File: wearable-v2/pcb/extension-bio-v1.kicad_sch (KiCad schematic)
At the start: 12 parts, among them J5 EXT_2_SOCKET, U11 TMP1075, U12 MAX30102

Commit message: Further V2 routing
Signed-off-by: Adam Fowler <adam@adamfowler.org>
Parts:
- H1: footprint Herald_Extras:MillSlot_8.0x1.0mm -> Herald:MillSlot_8.0x1.0mm
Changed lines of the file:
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@@
       (effects (font (size 1.27 1.27)) (justify left))
     )
-    (property "Footprint" "Herald_Extras:MillSlot_8.0x1.0mm" (at 78.74 171.45 0)
+    (property "Footprint" "Herald:MillSlot_8.0x1.0mm" (at 78.74 171.45 0)
       (effects (font (size 1.27 1.27)) hide)
     )

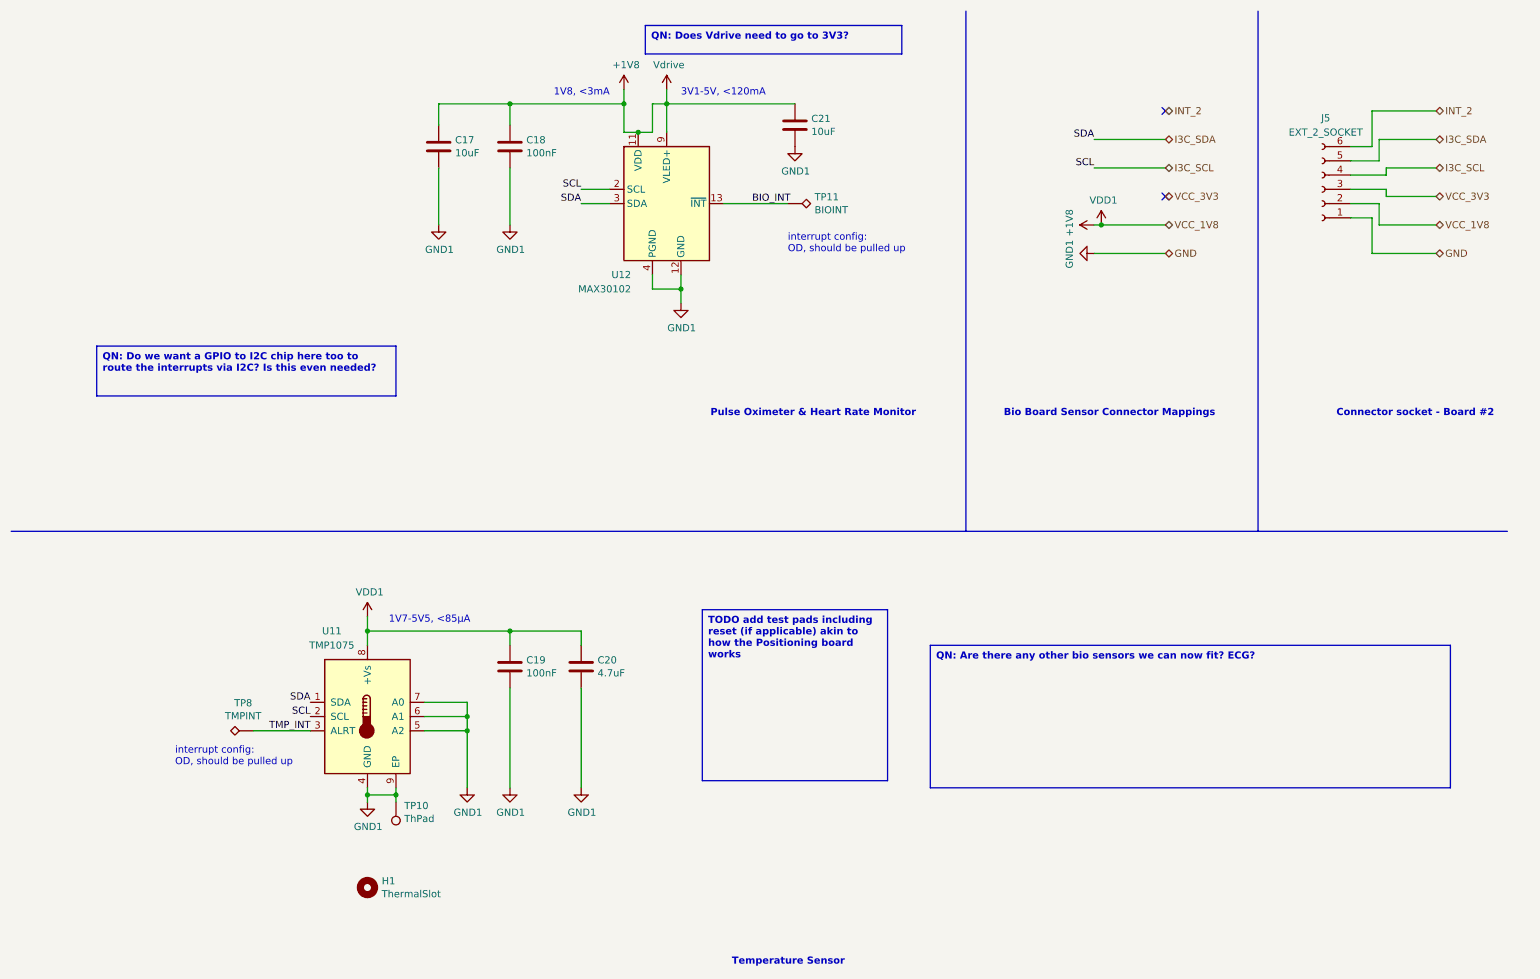
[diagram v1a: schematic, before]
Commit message: Added front connectors on main board
Signed-off-by: Adam Fowler <adam@adamfowler.org>
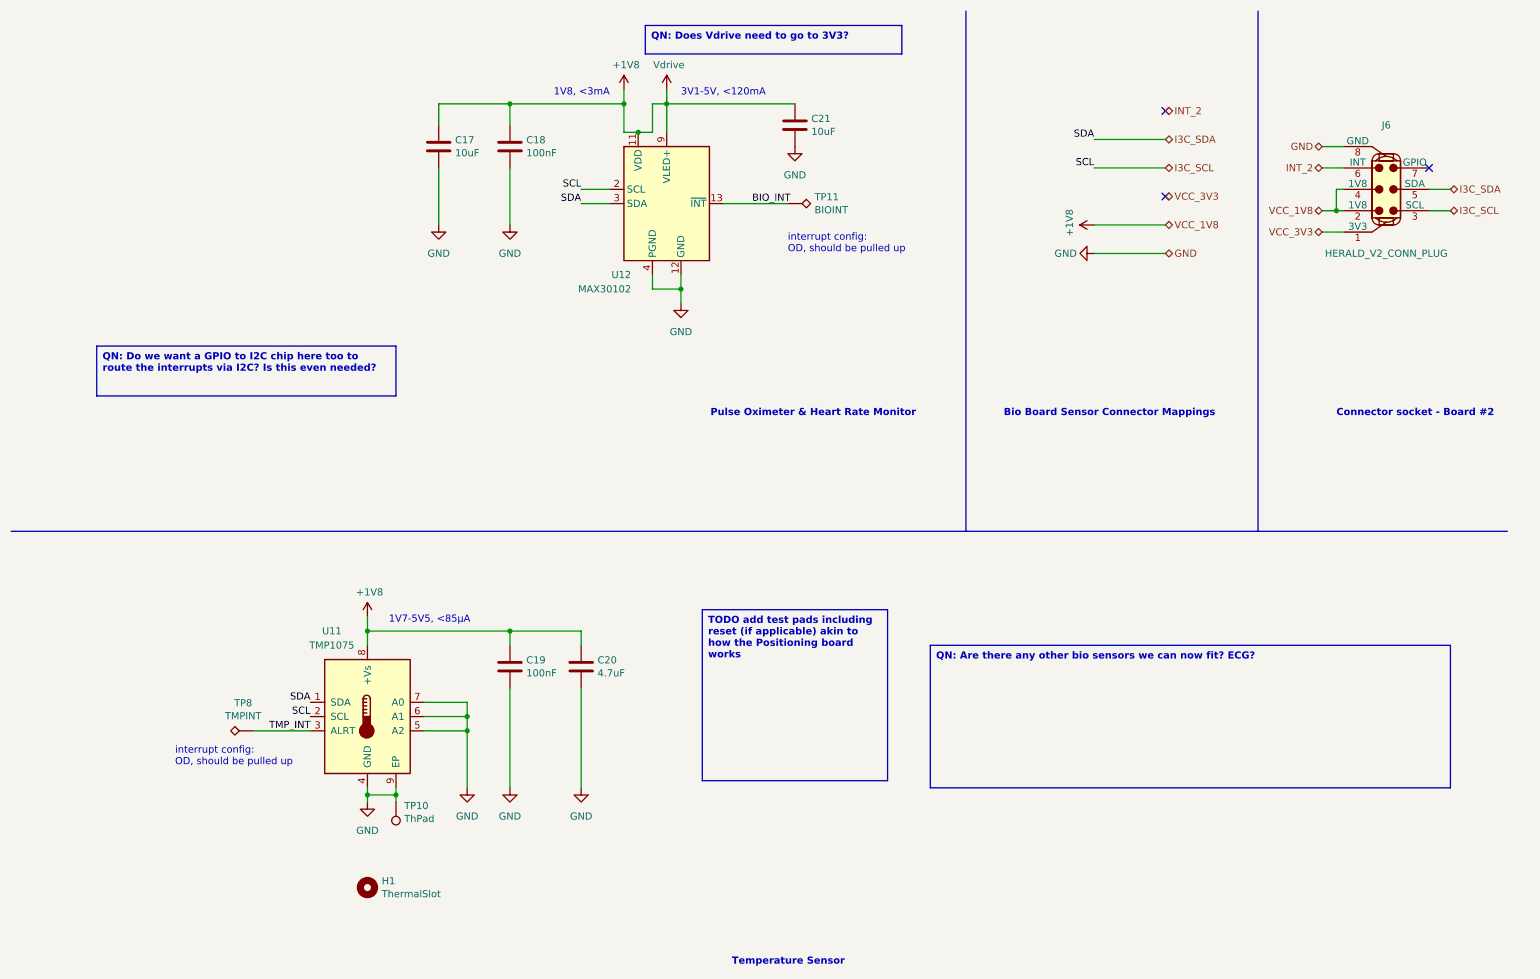
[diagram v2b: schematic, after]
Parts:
- removed J5: EXT_2_SOCKET, symbol Connector:Conn_01x06_Socket
- added J6: HERALD_V2_CONN_PLUG, symbol Herald_Extras:HERALD_V2_CONN_PLUG
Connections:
- net +1V8: now also J6.2 (1V8), J6.4 (1V8)
- net I3C_SCL: now also J6.3 (SCL)
- net I3C_SDA: now also J6.5 (SDA)
- net INT_2: now also J6.6 (INT)
- net VCC_3V3: now also J6.1 (3V3)
- net GND1 renamed GND
- net GND: now also J6.8 (GND)
- no-connect marks 2 -> 3

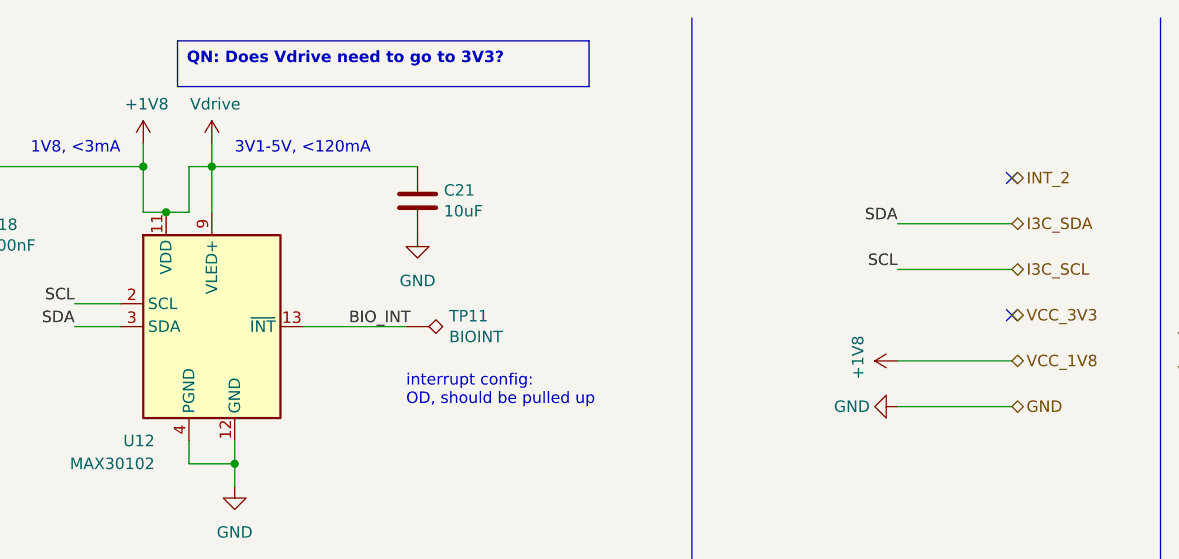
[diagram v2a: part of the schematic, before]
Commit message: Corrected 1V8 routing to bio board
Signed-off-by: Adam Fowler <adam@adamfowler.org>
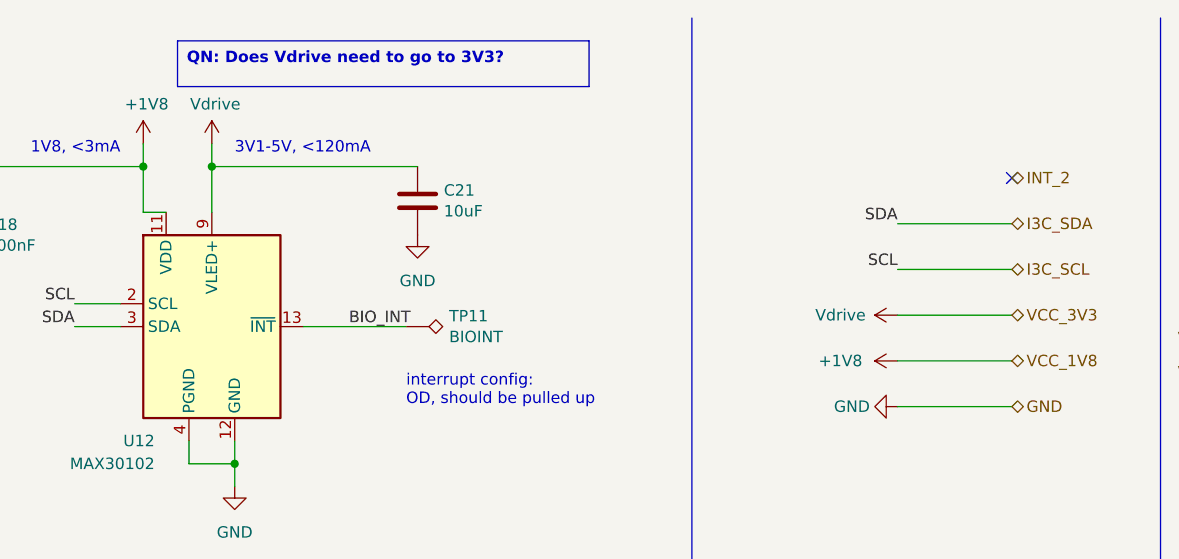
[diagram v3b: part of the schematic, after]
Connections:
- net +1V8: no longer C21.1, U12.10 (VLED+), U12.9 (VLED+)
- net VCC_3V3 renamed Vdrive
- net Vdrive: now also C21.1, U12.10 (VLED+), U12.9 (VLED+)
- no-connect marks 3 -> 2
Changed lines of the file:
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@@
   (junction (at 104.14 31.75) (diameter 0) (color 0 0 0 0)
   )
-  (junction (at 127 36.83) (diameter 0) (color 0 0 0 0)
-  )
   (junction (at 96.52 143.51) (diameter 0) (color 0 0 0 0)
   )
@@
   (junction (at 104.14 125.73) (diameter 0) (color 0 0 0 0)
   )
-  (no_connect (at 220.98 48.26))
   (no_connect (at 220.98 33.02))
   (no_connect (at 267.97 43.18))
@@
     (stroke (width 0) (type default))
   )
-  (wire (pts (xy 129.54 31.75) (xy 129.54 36.83))
-    (stroke (width 0) (type default))
-  )
   (wire (pts (xy 252.73 46.99) (xy 251.46 46.99))
     (stroke (width 0) (type default))
@@
     (stroke (width 0) (type default))
   )
-  (wire (pts (xy 132.08 31.75) (xy 129.54 31.75))
-    (stroke (width 0) (type default))
-  )
   (wire (pts (xy 267.97 46.99) (xy 271.78 46.99))
     (stroke (width 0) (type default))
@@
     (stroke (width 0) (type default))
   )
-  (wire (pts (xy 127 36.83) (xy 129.54 36.83))
+  (wire (pts (xy 208.28 48.26) (xy 220.98 48.26))
     (stroke (width 0) (type default))
   )
@@
         (path "/bdd943b2-035a-4beb-80ad-5c7e84260dde/00000000-0000-0000-0000-000060f1d377"
           (reference "U?") (unit 1)
+        )
+      )
+    )
+  )
+  (symbol (lib_id "power:Vdrive") (at 208.28 48.26 90) (unit 1)
+    (in_bom yes) (on_board yes) (dnp no)
+    (property "Reference" "#PWR059" (at 212.09 53.34 0)
+      (effects (font (size 1.27 1.27)) hide)
+    )
+    (property "Value" "Vdrive" (at 201.93 48.26 90)
+      (effects (font (size 1.27 1.27)))
+    )
+    (property "Footprint" "" (at 208.28 48.26 0)
+      (effects (font (size 1.27 1.27)) hide)
+    )
+    (property "Datasheet" "" (at 208.28 48.26 0)
+      (effects (font (size 1.27 1.27)) hide)
+    )
+    (pin "1")
+    (instances
+      (project "wearable-v2"
+        (path "/1eb7e8c9-86dc-4f6b-85aa-748b782af952/23d45666-f217-4505-adda-dcfbc4ac09cf"
+          (reference "#PWR059") (unit 1)
+        )
+      )
+      (project "wearable"
+        (path "/bdd943b2-035a-4beb-80ad-5c7e84260dde/00000000-0000-0000-0000-000060f4c181"
+          (reference "#PWR0119") (unit 1)
         )
       )
@@
       (effects (font (size 1.27 1.27)) hide)
     )
-    (property "Value" "+1V8" (at 203.8858 52.959 0)
-      (effects (font (size 1.27 1.27)))
-    )
+    (property "Value" "+1V8" (at 201.93 53.34 90)
+      (effects (font (size 1.27 1.27)))
+    )

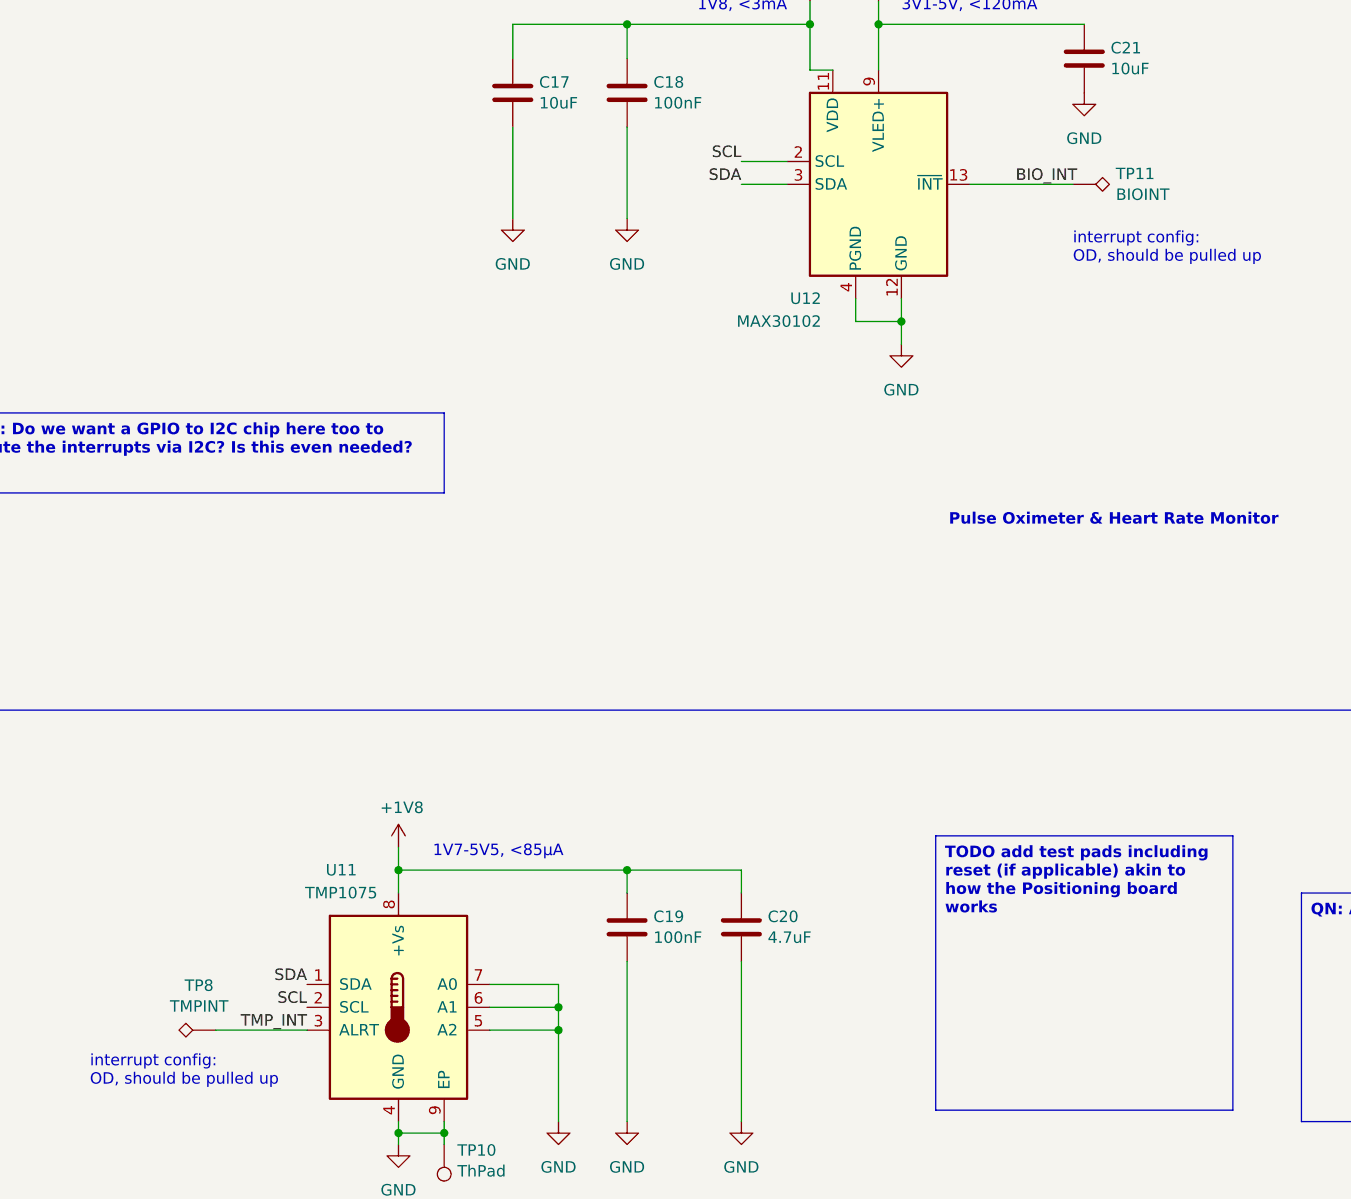
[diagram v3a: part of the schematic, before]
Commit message: Set wider PCB GND tracks and vias
Signed-off-by: Adam Fowler <adam@adamfowler.org>
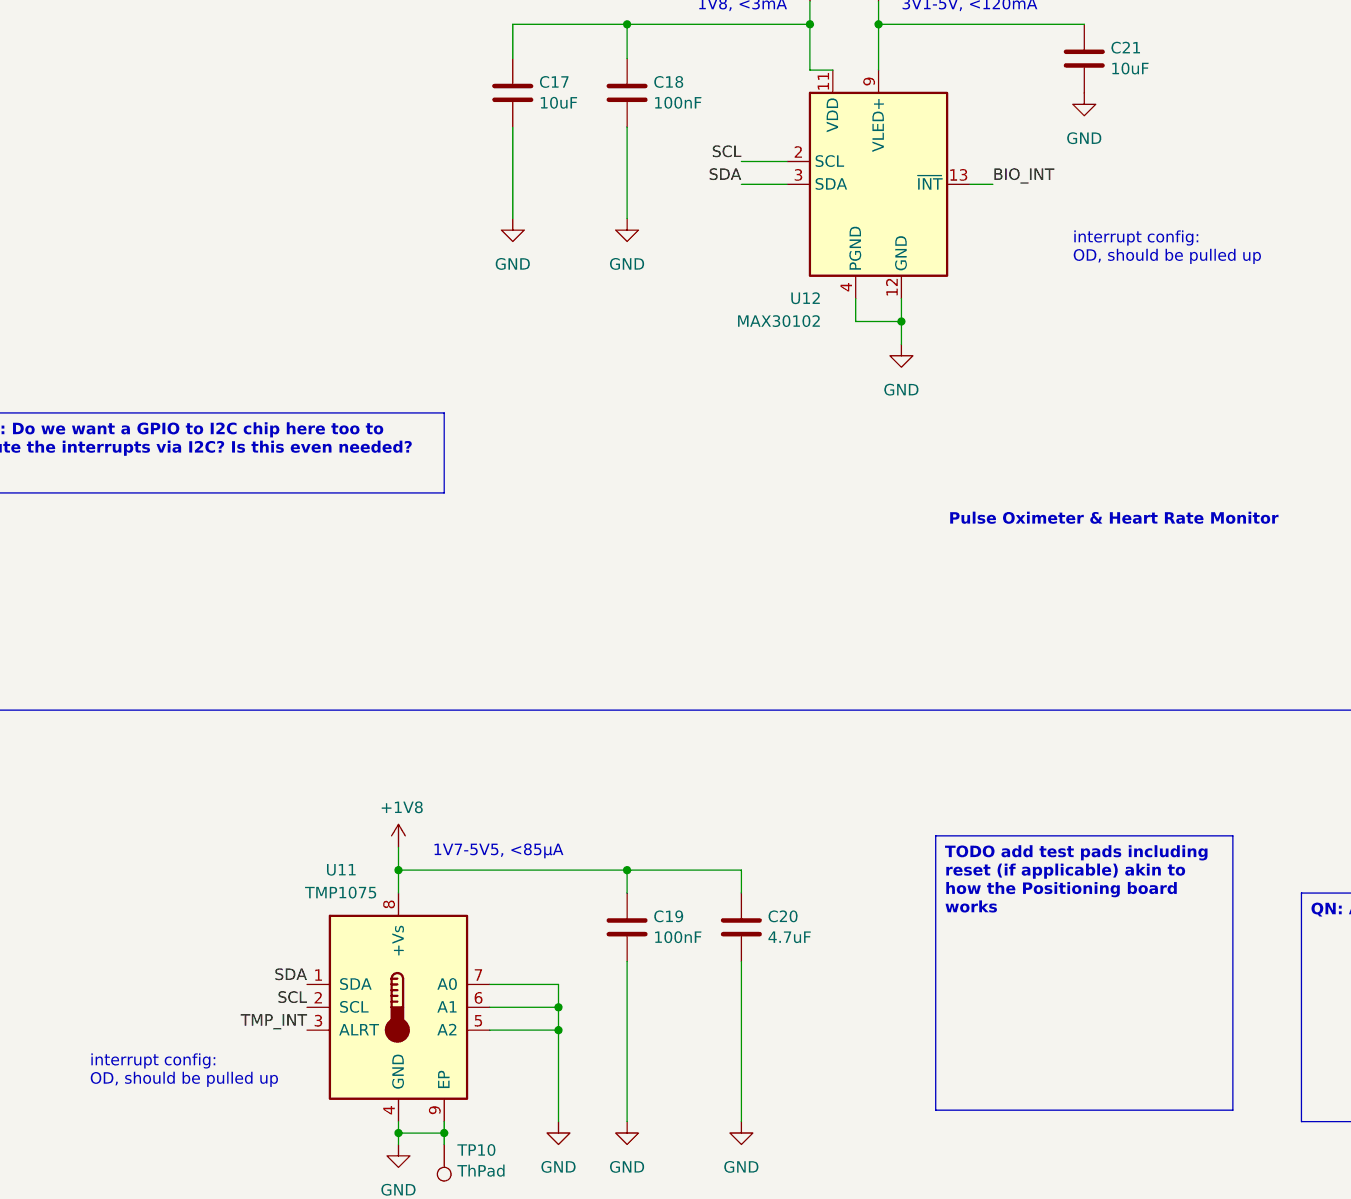
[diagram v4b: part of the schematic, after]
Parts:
- removed TP11: BIOINT, TestPoint:TestPoint_Pad_D1.0mm, symbol Connector:TestPoint_Alt
- removed TP8: TMPINT, TestPoint:TestPoint_Pad_D1.0mm, symbol Connector:TestPoint_Alt
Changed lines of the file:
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@@
     (stroke (width 0) (type default))
   )
-  (wire (pts (xy 142.24 49.53) (xy 153.67 49.53))
+  (wire (pts (xy 142.24 49.53) (xy 144.78 49.53))
     (stroke (width 0) (type default))
   )
@@
   )
   (polyline (pts (xy 185.42 15.24) (xy 185.42 107.95))
-    (stroke (width 0) (type default))
-  )
-  (wire (pts (xy 58.42 143.51) (xy 68.58 143.51))
     (stroke (width 0) (type default))
   )
@@
     (effects (font (size 1.27 1.27)) (justify right bottom))
   )
-  (label "BIO_INT" (at 147.32 49.53 0) (fields_autoplaced)
+  (label "BIO_INT" (at 144.78 49.53 0) (fields_autoplaced)
     (effects (font (size 1.27 1.27)) (justify left bottom))
   )
@@
     )
   )
-  (symbol (lib_id "Connector:TestPoint_Alt") (at 153.67 49.53 270) (unit 1)
-    (in_bom yes) (on_board yes) (dnp no)
-    (property "Reference" "TP11" (at 158.4452 48.3616 90)
-      (effects (font (size 1.27 1.27)) (justify left))
-    )
-    (property "Value" "BIOINT" (at 158.4452 50.673 90)
-      (effects (font (size 1.27 1.27)) (justify left))
-    )
-    (property "Footprint" "TestPoint:TestPoint_Pad_D1.0mm" (at 153.67 54.61 0)
-      (effects (font (size 1.27 1.27)) hide)
-    )
-    (property "Datasheet" "~" (at 153.67 54.61 0)
-      (effects (font (size 1.27 1.27)) hide)
-    )
-    (property "Description" "Test point" (at 153.67 49.53 0)
-      (effects (font (size 1.27 1.27)) hide)
-    )
-    (property "MPN" "~" (at 153.67 49.53 0)
-      (effects (font (size 1.27 1.27)) hide)
-    )
-    (pin "1")
-    (instances
-      (project "wearable-v2"
-        (path "/1eb7e8c9-86dc-4f6b-85aa-748b782af952/23d45666-f217-4505-adda-dcfbc4ac09cf"
-          (reference "TP11") (unit 1)
-        )
-      )
-      (project "wearable"
-        (path "/bdd943b2-035a-4beb-80ad-5c7e84260dde/00000000-0000-0000-0000-000060f4c181"
-          (reference "TP91") (unit 1)
-        )
-      )
-    )
-  )
   (symbol (lib_id "power:GND") (at 154.94 39.37 0) (unit 1)
     (in_bom yes) (on_board yes) (dnp no)
@@
         )
       )
-    )
-  )
-  (symbol (lib_id "Connector:TestPoint_Alt") (at 58.42 143.51 90) (unit 1)
-    (in_bom yes) (on_board yes) (dnp no)
-    (property "Reference" "TP8" (at 56.5912 138.557 90)
-      (effects (font (size 1.27 1.27)))
-    )
-    (property "Value" "TMPINT" (at 56.5912 140.8684 90)
-      (effects (font (size 1.27 1.27)))
-    )
-    (property "Footprint" "TestPoint:TestPoint_Pad_D1.0mm" (at 58.42 138.43 0)
-      (effects (font (size 1.27 1.27)) hide)
-    )
-    (property "Datasheet" "~" (at 58.42 138.43 0)
-      (effects (font (size 1.27 1.27)) hide)
-    )
-    (property "Description" "Test point" (at 58.42 143.51 0)
-      (effects (font (size 1.27 1.27)) hide)
-    )
-    (property "MPN" "~" (at 58.42 143.51 0)
-      (effects (font (size 1.27 1.27)) hide)
-    )
-    (pin "1")
-    (instances
-      (project "wearable-v2"
-        (path "/1eb7e8c9-86dc-4f6b-85aa-748b782af952/23d45666-f217-4505-adda-dcfbc4ac09cf"
-          (reference "TP8") (unit 1)
-        )
-      )
-      (project "wearable"
-        (path "/bdd943b2-035a-4beb-80ad-5c7e84260dde/00000000-0000-0000-0000-000060f4c181"
-          (reference "TP111") (unit 1)
-        )
-      )
